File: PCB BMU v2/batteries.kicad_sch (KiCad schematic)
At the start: 19 parts, among them Q8 IRFZ44NPBF, U7 INA237

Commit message: update code
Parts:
- removed Q8: IRFZ44NPBF, Package_TO_SOT_THT:TO-220-3_Horizontal_TabUp, symbol easyeda2kicad:IRFZ44NPBF
- removed R37: 10R, Resistor_SMD:R_0603_1608Metric, symbol Device:R_Small
- removed R40: 470R, Resistor_THT:R_Axial_DIN0204_L3.6mm_D1.6mm_P5.08mm_Horizontal, symbol Device:R_Small
- removed R41: 10k, Resistor_THT:R_Axial_DIN0204_L3.6mm_D1.6mm_P5.08mm_Horizontal, symbol Device:R_Small
- added Q1, Q13, Q17, Q18, Q19, Q20, Q5, Q9: IRF4905STRLPBF, easyeda2kicad:D2PAK_L9.1-W10.0-P2.54-LS15.3-TL, symbol easyeda2kicad:IRF4905STRLPBF
- C11: footprint Capacitor_SMD:C_0805_2012Metric -> Capacitor_SMD:C_0402_1005Metric; LCSC (none) -> C1525; LCSC Alt (none) -> C307331
- R38: value 10R -> 10K
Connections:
- net GND_BATT is gone; now on net GND: D16.1 (K), H4.1
- net +3.3V: now also R38.1
- net ALERT: now also R38.2
- net at R47.3: now also C10.1, U7.10 (Vin+)
- net at C10.2, U7.9 (Vin-): now also R47.4; no longer R38.1
- net +BATT_OUT: no longer names the net of R47.2
- net +BATT_OUT: now also Q1.3 (S), Q13.3 (S), Q17.4 (D), Q18.4 (D), Q19.4 (D), Q20.4 (D), Q5.3 (S), Q9.3 (S)
- new net: Q17.1 (G), Q18.1 (G), Q19.1 (G), Q20.1 (G)
- new net: Q1.1 (G), Q13.1 (G), Q5.1 (G), Q9.1 (G)
- new net +BATT OUT: Q1.4 (D), Q13.4 (D), Q17.3 (S), Q18.3 (S), Q19.3 (S), Q20.3 (S), Q5.4 (D), Q9.4 (D)
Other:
- note removed: "changer de ref de mosfet : a vérifier... IRFZ44NPBF"
- moved on the sheet: C10, C11, D14, D15, R39, R47, U7

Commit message: PCB update
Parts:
- removed Q1, Q13, Q17, Q18, Q19, Q20, Q5, Q9: IRF4905STRLPBF, easyeda2kicad:D2PAK_L9.1-W10.0-P2.54-LS15.3-TL, symbol easyeda2kicad:IRF4905STRLPBF
- added H18, H22: FH-00020, easyeda2kicad:HDR-TH_10P-P2.54-V-F-R2-C5-S2.54, symbol easyeda2kicad:FH-00020
- added H23: 12251103CNG0S115001, easyeda2kicad:HDR-TH_3P-P2.54-V-M-1, symbol easyeda2kicad:12251103CNG0S115001
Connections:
- net +3.3V: now also H23.1
- net +BATT OUT: now also H22.1, H22.10, H22.2, H22.3, H22.4, H22.5, H22.6, H22.7, H22.8, H22.9
- net GND: now also H23.3
- net +BATT_SHUNT_OUT: now reaches R47.2
- net +BATT_SHUNT_OUT: now also H18.1, H18.10, H18.2, H18.3, H18.4, H18.5, H18.6, H18.7, H18.8, H18.9
- net CMD_Switch_bat: now reaches D14.1 (K), D15.1 (K), R39.2
- net CMD_Switch_bat: now also H23.2
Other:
- moved on the sheet: D14, D15, D16, R39

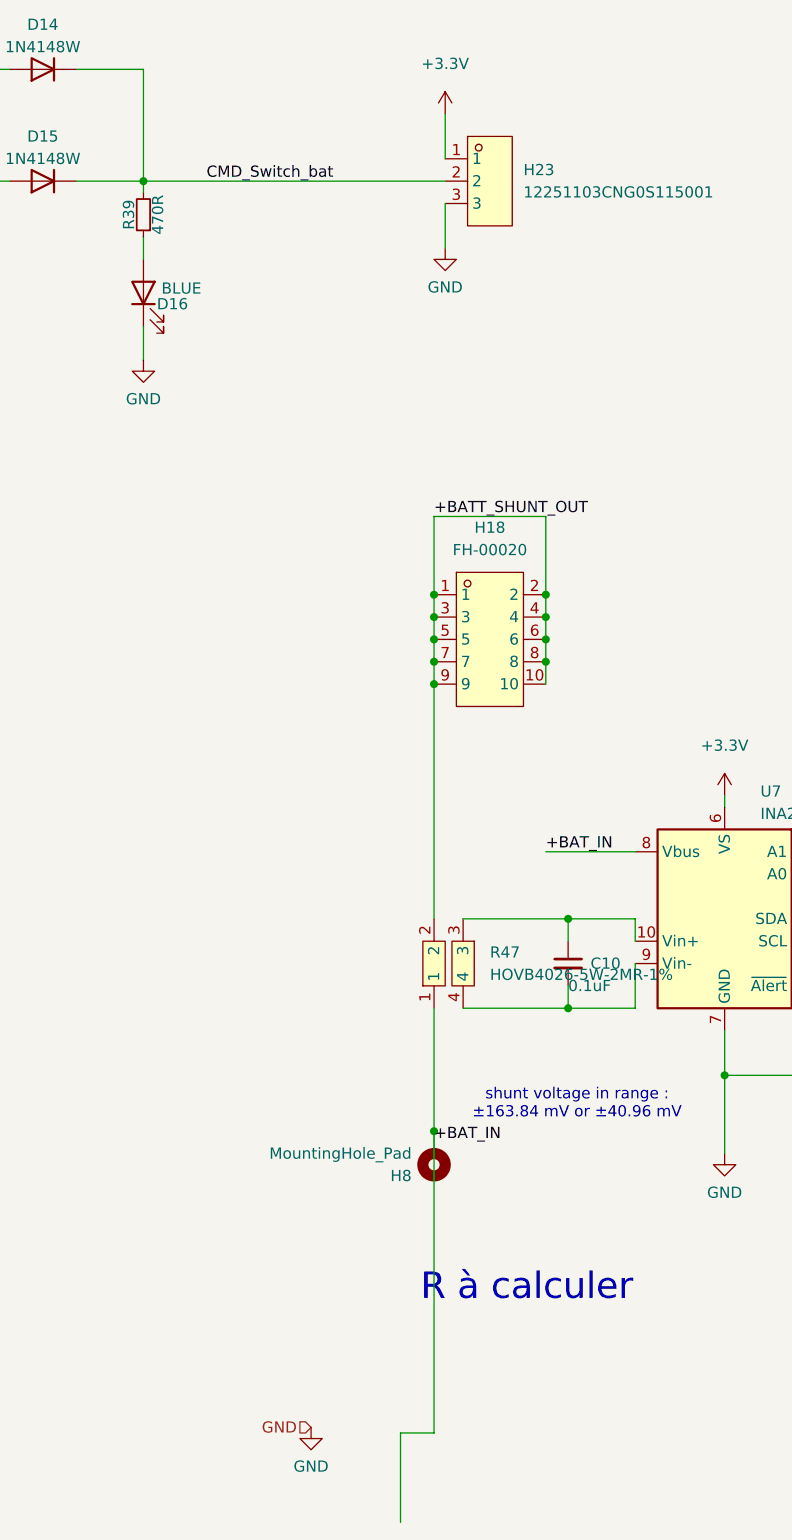
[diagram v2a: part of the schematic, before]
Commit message: add Ampère/Houre calculation
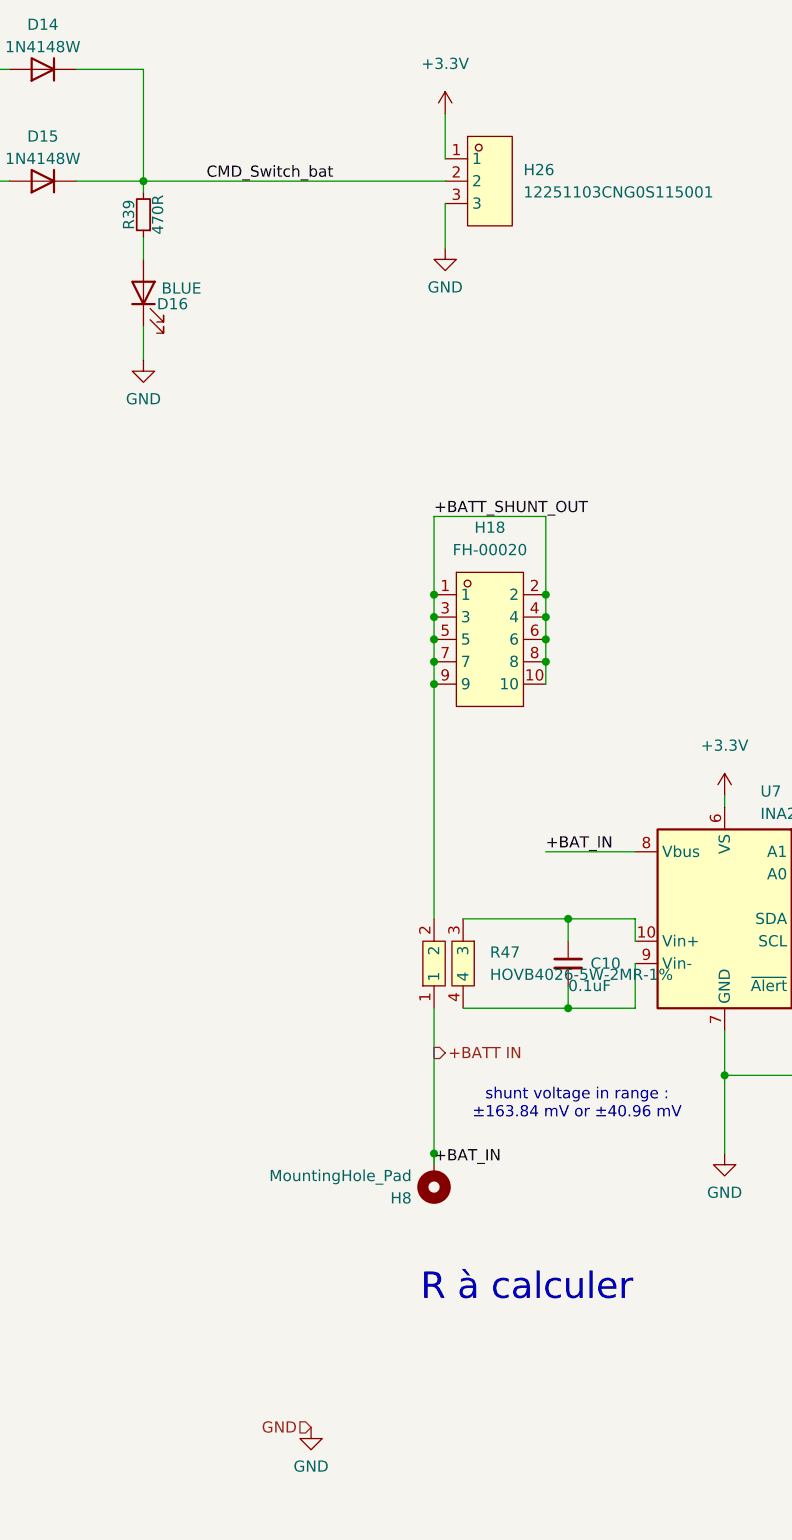
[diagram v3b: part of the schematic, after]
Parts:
- renumbered H23 to H26
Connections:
- net +BAT_IN renamed +BATT IN
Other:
- moved on the sheet: H8
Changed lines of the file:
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@@
 	)
 	(junction
-		(at 184.15 157.48)
+		(at 184.15 104.14)
 		(diameter 0)
 		(color 0 0 0 0)
 	)
 	(junction
-		(at 184.15 104.14)
+		(at 237.49 99.06)
 		(diameter 0)
 		(color 0 0 0 0)
 	)
 	(junction
-		(at 237.49 99.06)
+		(at 237.49 101.6)
 		(diameter 0)
 		(color 0 0 0 0)
 	)
 	(junction
-		(at 237.49 101.6)
+		(at 184.15 160.02)
 		(diameter 0)
 		(color 0 0 0 0)
@@
 	(wire
 		(pts
-			(xy 180.34 191.77) (xy 184.15 191.77)
-		)
-		(stroke
-			(width 0)
-			(type default)
-		)
-	)
-	(wire
-		(pts
 			(xy 196.85 101.6) (xy 196.85 104.14)
 		)
@@
 	(wire
 		(pts
-			(xy 184.15 157.48) (xy 184.15 143.51)
+			(xy 184.15 143.51) (xy 184.15 160.02)
 		)
 		(stroke
@@
 	(wire
 		(pts
-			(xy 180.34 201.93) (xy 180.34 191.77)
+			(xy 184.15 161.29) (xy 184.15 160.02)
 		)
 		(stroke
@@
 	(wire
 		(pts
-			(xy 184.15 157.48) (xy 184.15 191.77)
-		)
-		(stroke
-			(width 0)
-			(type default)
-		)
-	)
-	(wire
-		(pts
 			(xy 185.42 57.15) (xy 185.42 52.07)
 		)
@@
 	)
 	(label "+BAT_IN"
-		(at 184.15 158.75 0)
+		(at 184.15 161.29 0)
 		(fields_autoplaced yes)
 		(effects
@@
 		)
 	)
+	(hierarchical_label "+BATT IN"
+		(shape output)
+		(at 184.15 148.59 0)
+		(fields_autoplaced yes)
+		(effects
+			(font
+				(size 1.27 1.27)
+			)
+			(justify left)
+		)
+	)
 	(hierarchical_label "+BATT OUT"
 		(shape output)
@@
 		(dnp no)
 		(fields_autoplaced yes)
-		(property "Reference" "#PWR094"
+		(property "Reference" "#PWR0100"
 			(at 185.42 45.72 0)
 			(effects
@@
 	(symbol
 		(lib_id "Mechanical:MountingHole_Pad")
-		(at 184.15 160.02 180)
+		(at 184.15 162.56 180)
 		(unit 1)
 		(exclude_from_sim yes)
@@
 		(fields_autoplaced yes)
 		(property "Reference" "H8"
-			(at 181.61 162.5601 0)
+			(at 181.61 165.1001 0)
 			(effects
 				(font
@@
 		)
 		(property "Value" "MountingHole_Pad"
-			(at 181.61 160.0201 0)
+			(at 181.61 162.5601 0)
 			(effects
 				(font
@@
 		)
 		(property "Footprint" "MountingHole:MountingHole_5mm_Pad"
-			(at 184.15 160.02 0)
+			(at 184.15 162.56 0)
 			(effects
 				(font
@@
 		)
 		(property "Datasheet" "~"
-			(at 184.15 160.02 0)
+			(at 184.15 162.56 0)
 			(effects
 				(font
@@
 		)
 		(property "Description" "Mounting Hole with connection"
-			(at 184.15 160.02 0)
+			(at 184.15 162.56 0)
 			(effects
 				(font
@@
 		(dnp no)
 		(fields_autoplaced yes)
-		(property "Reference" "H23"
+		(property "Reference" "H26"
 			(at 194.31 48.2599 0)
 			(effects
